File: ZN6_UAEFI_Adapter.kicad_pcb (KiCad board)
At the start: 4 copper layers, 160 x 170 mm, 48 parts, among them J1 Conn_01x32_Socket, J12 Conn_01x06_Socket, J13 Conn_01x06_Socket, J14 Conn_01x06_Socket, J2 Conn_01x32_Socket, J3 Conn_01x02_Socket, J4 Conn_01x24_Socket, J5 Conn_01x24_Socket, Q1 NCV8402ADDR2G, U2 ADS7128IRTER, U3 MIC5205-3.3YM5

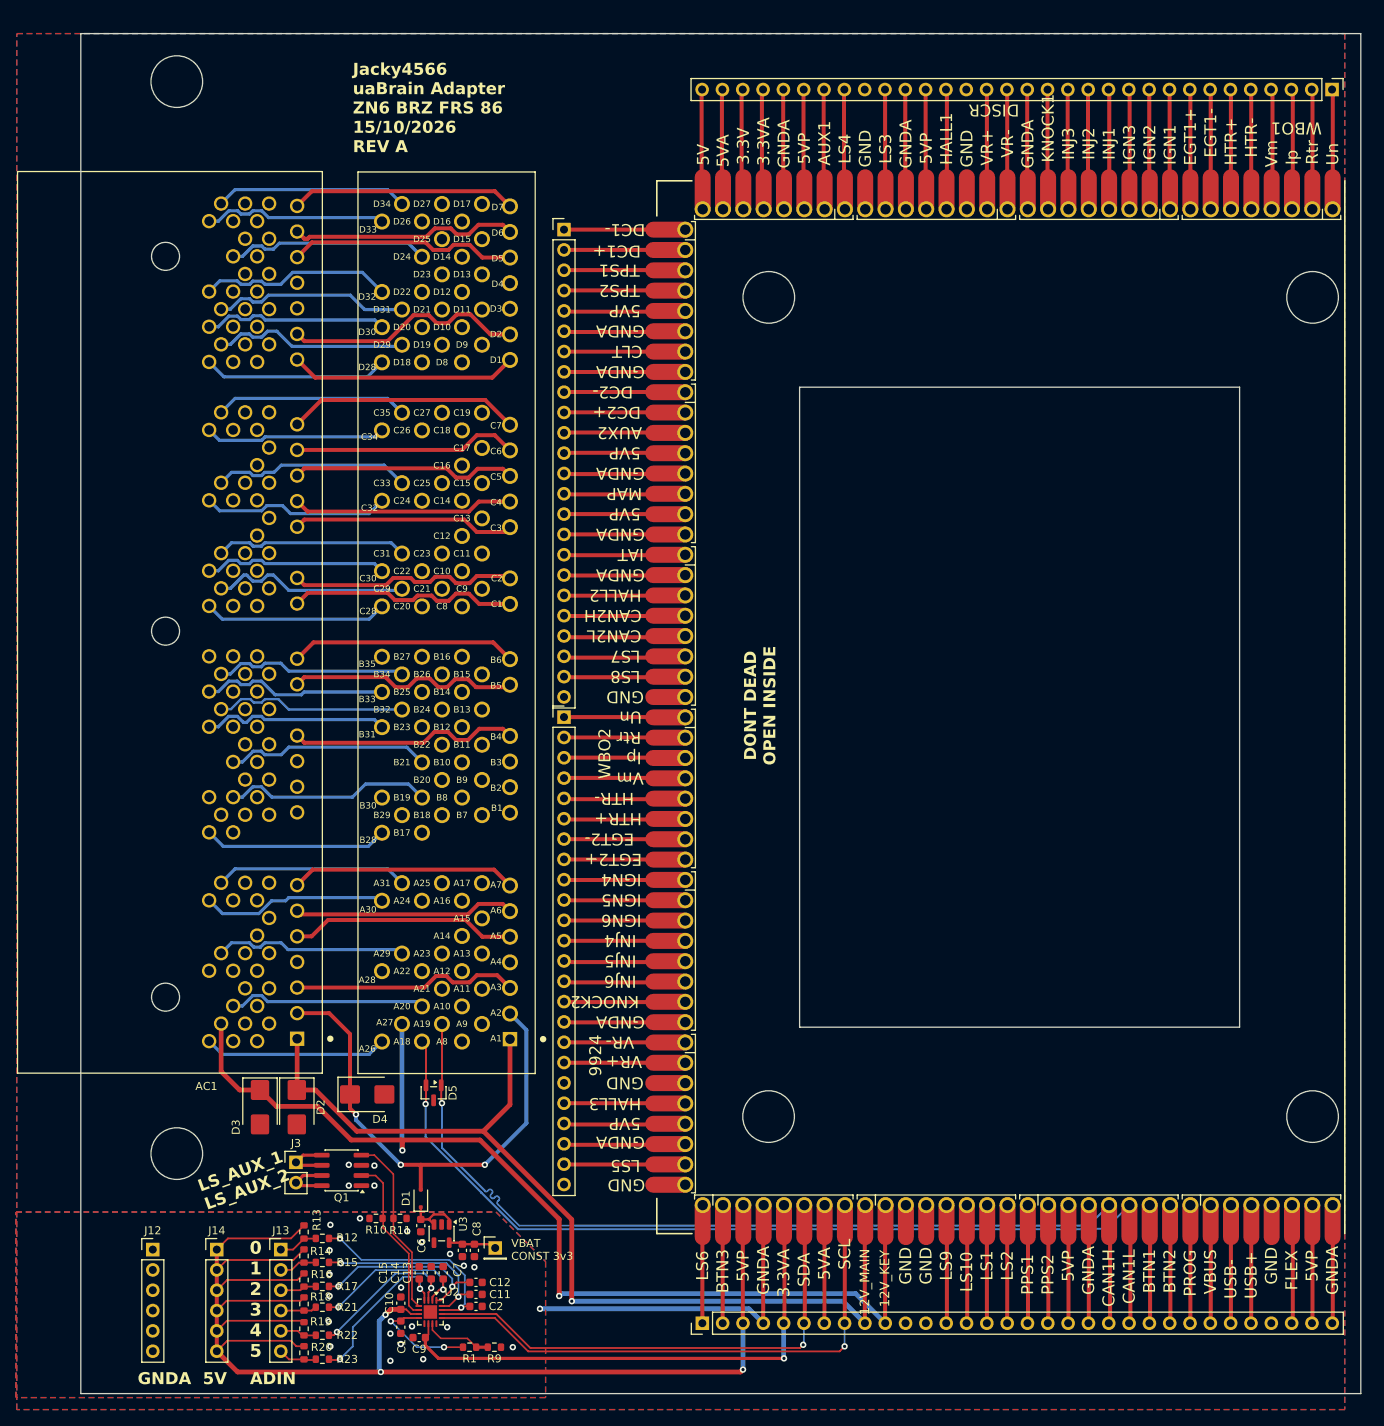
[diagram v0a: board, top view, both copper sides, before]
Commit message: Re-adjust project for uaEFI instead.
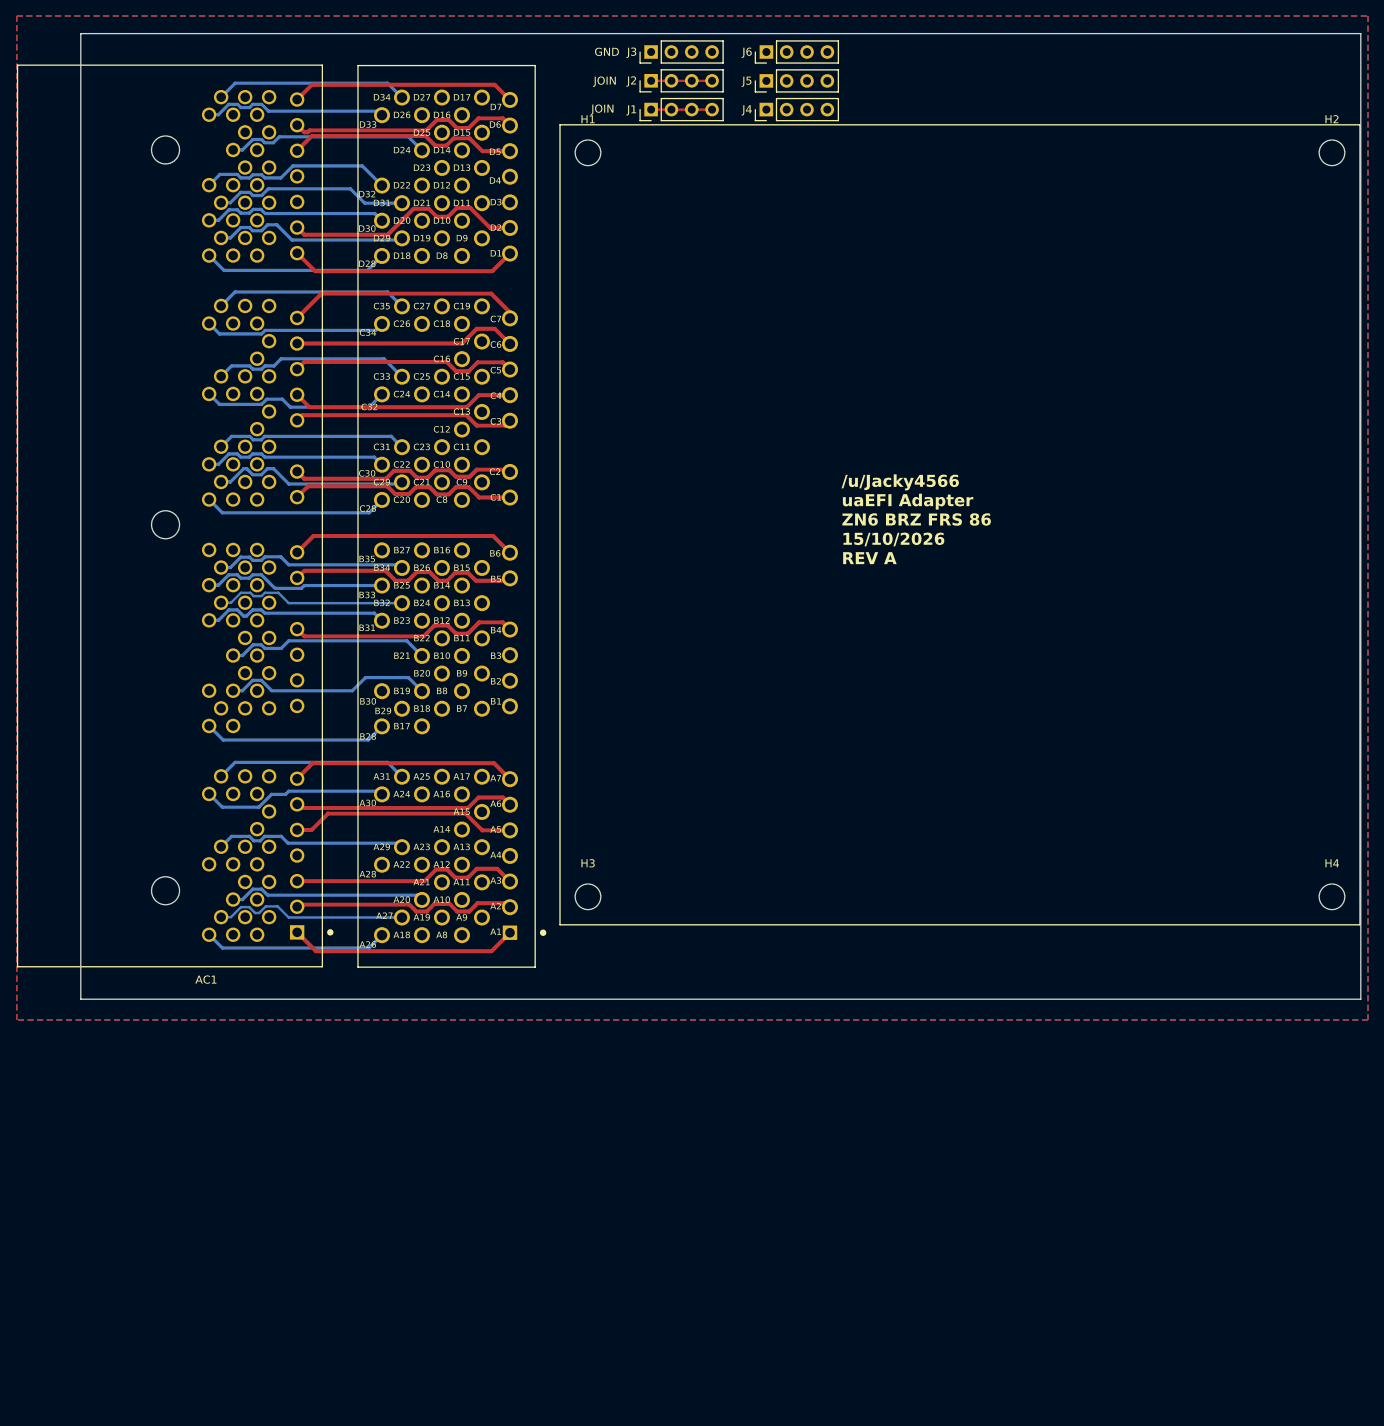
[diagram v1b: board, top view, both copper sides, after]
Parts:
- removed C1, C10, C6, C7, C9: 1uF, Capacitor_SMD:C_0603_1608Metric
- removed C11, C12, C13, C14, C15, C2: 10nF, Capacitor_SMD:C_0603_1608Metric
- removed C8: 10uF, Capacitor_SMD:C_0603_1608Metric
- removed D1: 1N4148WS, Diode_SMD:D_SOD-323F
- removed D2, D3, D4: SMBJ24A, Diode_SMD:D_SMB
- removed D5: SZNUP2105L, Package_TO_SOT_SMD:SOT-23
- removed J12, J13, J14: Conn_01x06_Socket, Connector_PinHeader_2.54mm:PinHeader_1x06_P2.54mm_Vertical
- removed Q1: NCV8402ADDR2G, Package_SO:SOIC-8_3.9x4.9mm_P1.27mm
- removed R1: 11k, Resistor_SMD:R_0603_1608Metric
- removed R10, R11, R13, R14, R16, R18, R19, R20: 10k, Resistor_SMD:R_0603_1608Metric
- removed R12, R15, R17, R21, R22, R23: 4.7k, Resistor_SMD:R_0603_1608Metric
- removed R9: DNP, Resistor_SMD:R_0603_1608Metric
- removed TP1: VBAT, Connector_PinHeader_2.54mm:PinHeader_1x01_P2.54mm_Vertical
- removed U2: ADS7128IRTER, Package_DFN_QFN:WQFN-16-1EP_3x3mm_P0.5mm_EP1.68x1.68mm
- removed U3: MIC5205-3.3YM5, Package_TO_SOT_SMD:SOT-23-5
- removed hw-uaBrain1: hw-uaBrain, ZN6:hw-uaBrain
- added H1: MountingHole, MountingHole:MountingHole_3.2mm_M3, F.Cu at (107.4, 64.9)
- added H2: MountingHole, MountingHole:MountingHole_3.2mm_M3, F.Cu at (200.4, 64.9)
- added H3: MountingHole, MountingHole:MountingHole_3.2mm_M3, F.Cu at (107.4, 157.9)
- added H4: MountingHole, MountingHole:MountingHole_3.2mm_M3, F.Cu at (200.4, 157.9)
- added J6: Conn_01x04_Socket, Connector_PinHeader_2.54mm:PinHeader_1x04_P2.54mm_Vertical, F.Cu at (129.7, 52.3)
- J1, J2: value Conn_01x32_Socket -> Conn_01x04_Socket; footprint Connector_PinHeader_2.54mm:PinHeader_1x32_P2.54mm_Vertical -> Connector_PinHeader_2.54mm:PinHeader_1x04_P2.54mm_Vertical
- J3: value Conn_01x02_Socket -> Conn_01x04_Socket; footprint Connector_PinHeader_2.54mm:PinHeader_1x02_P2.54mm_Vertical -> Connector_PinHeader_2.54mm:PinHeader_1x04_P2.54mm_Vertical
- J4, J5: value Conn_01x24_Socket -> Conn_01x04_Socket; footprint Connector_PinHeader_2.54mm:PinHeader_1x24_P2.54mm_Vertical -> Connector_PinHeader_2.54mm:PinHeader_1x04_P2.54mm_Vertical
- moved J2 155.4 mm to (115.3, 55.9)
- moved J3 145.7 mm to (115.3, 52.3), turned to 90 degrees
- moved J1 85.2 mm to (115.3, 59.5), turned to 90 degrees
- moved J5 83.5 mm to (129.7, 55.9), turned to 90 degrees
- moved J4 29.4 mm to (129.7, 59.5), turned to 90 degrees
- moved AC2 13.3 mm to (86.6, 162.7)
- moved AC1 13.3 mm to (60.0, 162.6)
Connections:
- net /+12V_CONSTANT renamed Net-(AC1-Pad2)
- AC1 pad 1: /+12V -> Net-(AC1-Pad1)
- AC1 pad 104: GND -> /GND
- AC1 pad 105: GND -> /GND
- AC1 pad 27: /12V_KEY -> Net-(AC1-Pad27)
- AC1 pad 28: GND -> /GND
- AC1 pad 32: GND -> /GND
- AC1 pad 33: GND -> /GND
- AC1 pad 34: GND -> /GND
- AC1 pad 4: GND -> /GND
- AC1 pad 60: GND -> /GND
- AC1 pad 61: GND -> /GND
- AC1 pad 66: GND -> /GND
- AC2 pad 1: /+12V -> Net-(AC1-Pad1)
- AC2 pad 104: GND -> /GND
- AC2 pad 105: GND -> /GND
- AC2 pad 27: /12V_KEY -> Net-(AC1-Pad27)
- AC2 pad 28: GND -> /GND
- AC2 pad 32: GND -> /GND
- AC2 pad 33: GND -> /GND
- AC2 pad 34: GND -> /GND
- AC2 pad 4: GND -> /GND
- AC2 pad 60: GND -> /GND
- AC2 pad 61: GND -> /GND
- AC2 pad 66: GND -> /GND
- J1 pad 2: Net-(J1-Pin_2) -> Net-(J1-Pin_1)
- J1 pad 3: Net-(J1-Pin_3) -> Net-(J1-Pin_1)
- J1 pad 4: Net-(J1-Pin_4) -> Net-(J1-Pin_1)
- J2 pad 2: Net-(J2-Pin_2) -> Net-(J2-Pin_1)
- J2 pad 3: /5VP -> Net-(J2-Pin_1)
- J2 pad 4: GNDA -> Net-(J2-Pin_1)
- J3 pad 1: /ADS712/LS_AUX_1 -> /GND
- J3 pad 2: /ADS712/LS_AUX_2 -> /GND
- J4 pad 1: Net-(J4-Pin_1) -> unconnected-(J4-Pin_1-Pad1)
- J4 pad 2: Net-(J4-Pin_2) -> unconnected-(J4-Pin_2-Pad2)
- J4 pad 3: Net-(J4-Pin_3) -> unconnected-(J4-Pin_3-Pad3)
- J4 pad 4: Net-(J4-Pin_4) -> unconnected-(J4-Pin_4-Pad4)
- J5 pad 1: Net-(J5-Pin_1) -> unconnected-(J5-Pin_1-Pad1)
- J5 pad 2: Net-(J5-Pin_2) -> unconnected-(J5-Pin_2-Pad2)
- J5 pad 3: Net-(J5-Pin_3) -> unconnected-(J5-Pin_3-Pad3)
- J5 pad 4: Net-(J5-Pin_4) -> unconnected-(J5-Pin_4-Pad4)
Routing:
- net /5VP: track 181.5 -> 0.00 mm, vias 3 -> 0
- net /12V_KEY: track 138.3 -> 0.00 mm, vias 2 -> 0
- net /+12V: track 122.2 -> 0.00 mm, vias 1 -> 0
- net /CAN1+: track 148.7 -> 29.5 mm, vias 1 -> 0
- net /CAN1-: track 144.8 -> 29.5 mm, vias 1 -> 0
- net /SCL: track 68.4 -> 0.00 mm, vias 1 -> 0
- net /+3.3VA: track 65.9 -> 0.00 mm, vias 1 -> 0
- net /SDA: track 63.0 -> 0.00 mm, vias 1 -> 0
- net GNDA: track 41.8 -> 0.00 mm, vias 21 -> 0
- net Net-(AC1-Pad2): track 62.2 -> 28.5 mm, vias 3 -> 0
- net Net-(AC1-Pad1): track 0.00 -> 28.5 mm
- net /ADS712/AIN0: track 26.8 -> 0.00 mm, vias 2 -> 0
- net Net-(AC1-Pad27): track 0.00 -> 24.3 mm
- net /ADS712/AIN1: track 23.6 -> 0.00 mm, vias 2 -> 0
- net /ADS712/AIN2: track 23.3 -> 0.00 mm, vias 2 -> 0
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- added copper zone on B.Cu, net /GND
- added copper zone on F.Cu, net /GND
- added copper zone on In1.Cu, net /GND
- added copper zone on In2.Cu, net /GND
- removed copper zone on B.Cu, net GND
- removed copper zone on F.Cu, net GND
- removed copper zone on In1.Cu, net GND
- removed copper zone on In2.Cu, net GND
- removed copper zone on B.Cu, net GNDA
- removed copper zone on F.Cu, net GNDA
- removed copper zone on In1.Cu, net GNDA
- removed copper zone on In2.Cu, net GNDA
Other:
- board size 160 x 170 mm -> 160 x 120.7 mm
- board text added: "/u/Jacky4566 uaEFI Adapter ZN6 BRZ FRS 86 15/10/2026 REV A"
- board text added: "GND"
- board text added: "JOIN"
- board text removed: "0 1 2 3 4 5"
- board text removed: "DONT DEAD OPEN INSIDE"
- board text removed: "GNDA 5V ADIN"
- board text removed: "Jacky4566 uaBrain Adapter ZN6 BRZ FRS 86 15/10/2026 REV A"
- board text removed: "LS_AUX_1 LS_AUX_2"
- board text removed: "VBAT CONST 3v3"

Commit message: Update Image
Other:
- board text added: "/u/Jacky4566 uaEFI Adapter ZN6 BRZ FRS 86 REV A"
- board text removed: "/u/Jacky4566 uaEFI Adapter ZN6 BRZ FRS 86 15/10/2026 REV A"
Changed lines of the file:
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@@
 		)
 	)
-	(gr_text "/u/Jacky4566\nuaEFI Adapter\nZN6 BRZ FRS 86\n15/10/2026\nREV A"
+	(gr_text "/u/Jacky4566\nuaEFI Adapter\nZN6 BRZ FRS 86\nREV A"
 		(at 139.1 116.5 0)
 		(layer "F.SilkS")
